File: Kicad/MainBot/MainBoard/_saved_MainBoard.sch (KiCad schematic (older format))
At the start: 83 parts, among them J1 02x04_I2C, J13 01x02, J14 01x02_DAC, J16 Conn_01x24, J17 Conn_01x24, J18 01x24, J19 01x24, J2 02x03, J20 01x05, J21 01x03, J22 Conn_01x03, J23 Conn_01x03, J24 01x04, J25 01x03, J26 Conn_01x04, J27 01x04, J28 Conn_01x02, J3 02x03, J30 Conn_01x03, J43 Conn_01x03, J44 Conn_01x02, J45 Conn_01x02, J46 Conn_01x02, J47 Conn_01x02, J48 Conn_01x03, J49 Conn_01x04, J50 Conn_01x03, J51 01x04, J52 01x04, J53 01x04, J54 01x04, U1 AZ1117-3.3, U2 TCA9548A, U3 Teensy3.6, U4 DRV8825, U5 DRV8825, U6 DRV8825, U7 DRV8825

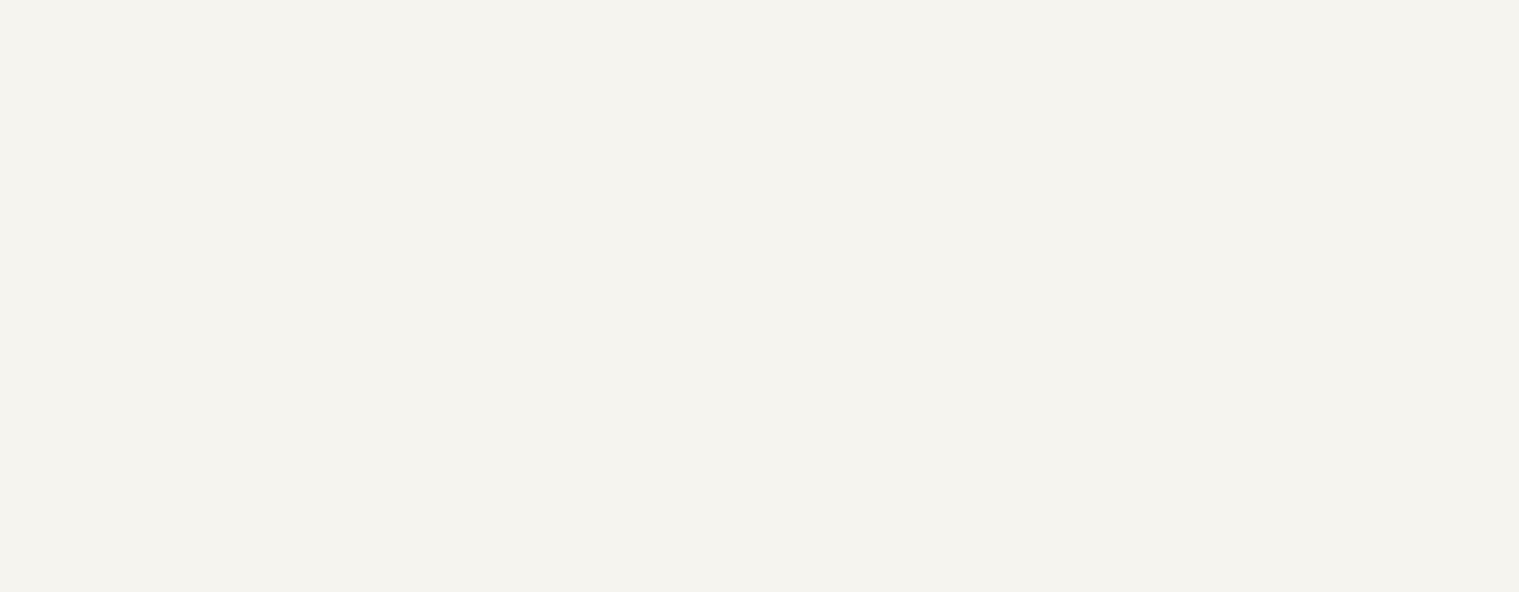
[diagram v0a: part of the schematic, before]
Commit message: Corrected Reverse-current protection, replaced regulator with 3.3V Step-Down Buck Converter
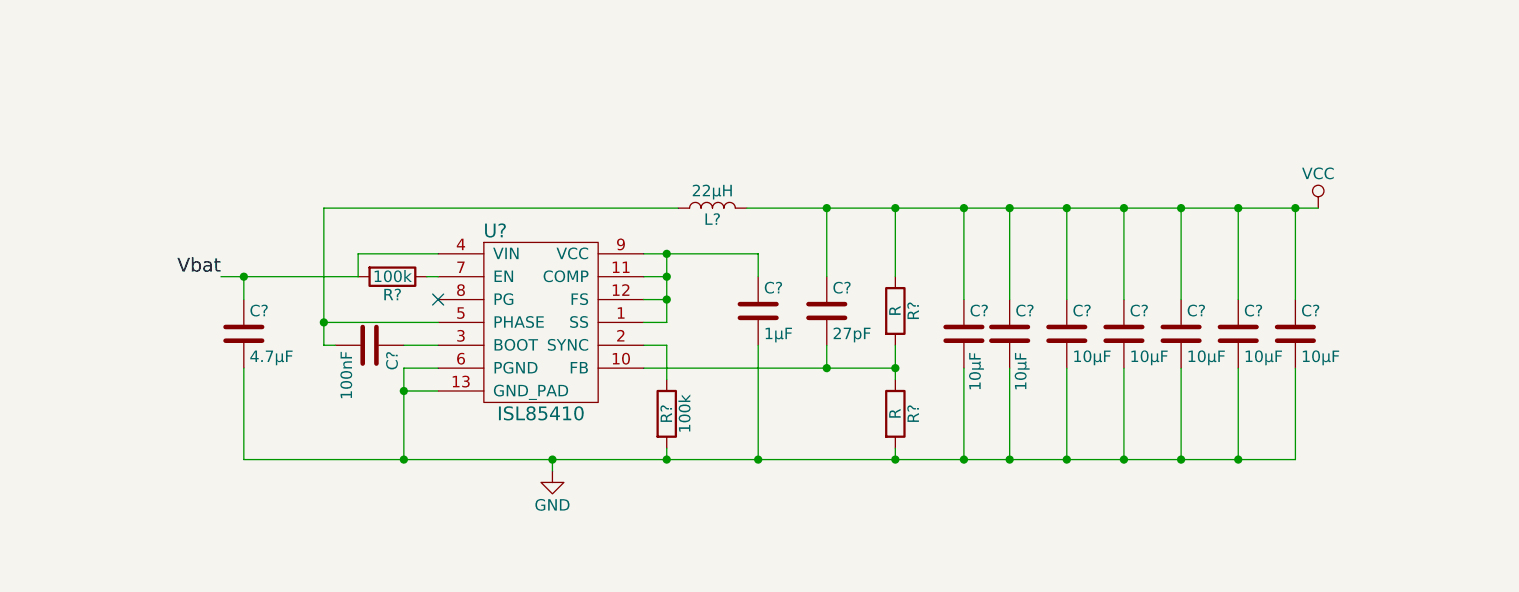
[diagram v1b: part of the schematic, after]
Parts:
- added 100k: R?, symbol R
- added C?: 1µF, symbol C
- added C?: 27pF, symbol C
- added C?: 100nF, symbol C
- added C?: 4.7µF, symbol C
- added C? (x7): 10µF, symbol C
- added L?: 22µH, symbol L
- added R? (x2): R, symbol R
- added R?: 100k, symbol R
- added U?: ISL85410, symbol ISL85410
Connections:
- net +12C: now also C?.1, R?.2, U?.4 (VIN)
- net GND: now also 100k.2, C?.2, C?.2, C?.2, C?.2, C?.2, C?.2, C?.2, C?.2, C?.2, R?.2, U?.13 (GND_PAD), U?.6 (PGND)
- net VCC: now also C?.1, C?.1, C?.1, C?.1, C?.1, C?.1, C?.1, C?.1, L?.2, R?.1
- new net: C?.1, U?.1 (SS), U?.11 (COMP), U?.12 (FS), U?.9 (VCC)
- new net: C?.2, R?.1, R?.2, U?.10 (FB)
- new net: 100k.1, U?.2 (SYNC)
- new net: C?.1, U?.3 (BOOT)
- new net: C?.2, L?.1, U?.5 (PHASE)
- new net: R?.1, U?.7 (EN)
- no-connect marks 7 -> 8
